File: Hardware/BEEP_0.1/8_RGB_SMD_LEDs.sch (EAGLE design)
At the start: 34 parts

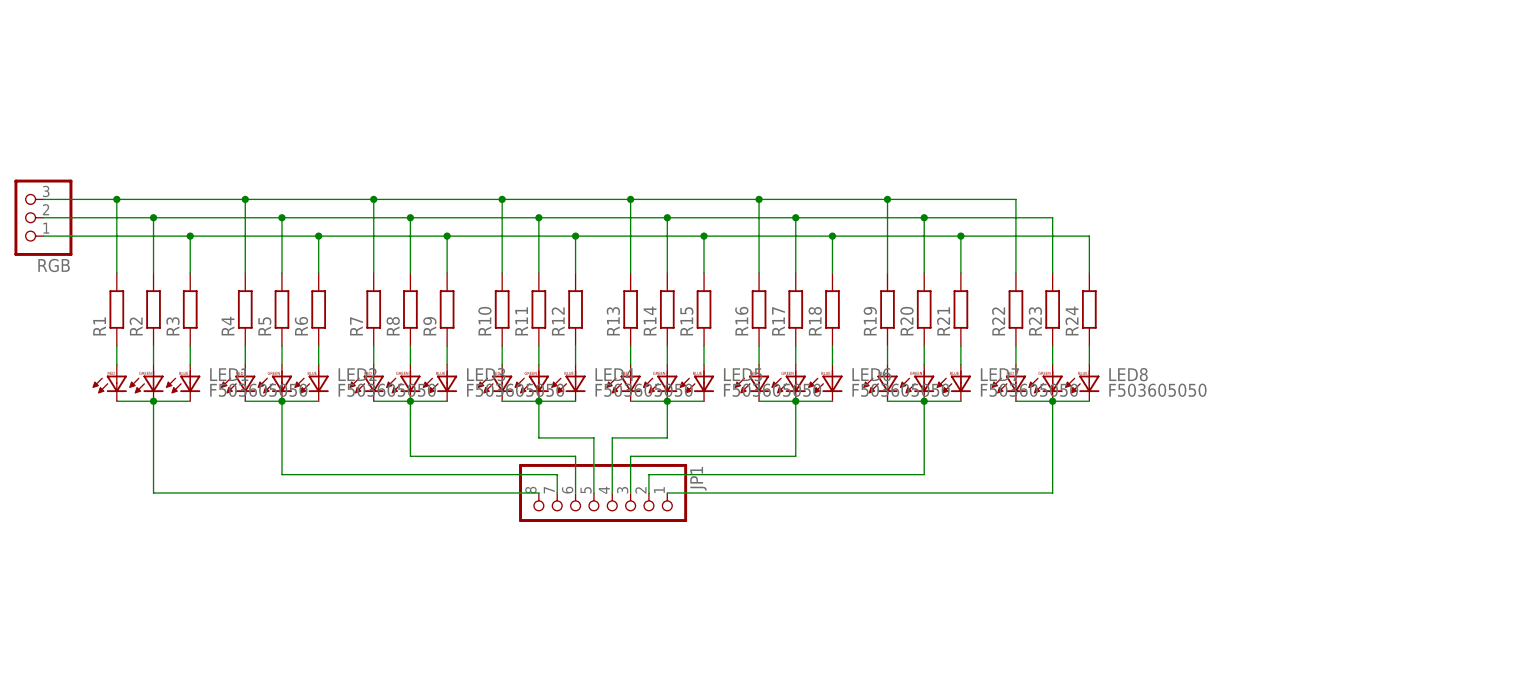
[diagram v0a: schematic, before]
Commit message: Add branding ;) enhance PCBs finish Easy RGB Board add Texas Instruments libray from Element 14 add dxf import ulp for eagle add Script for easy eagle export to pdf for etching minor cleanup
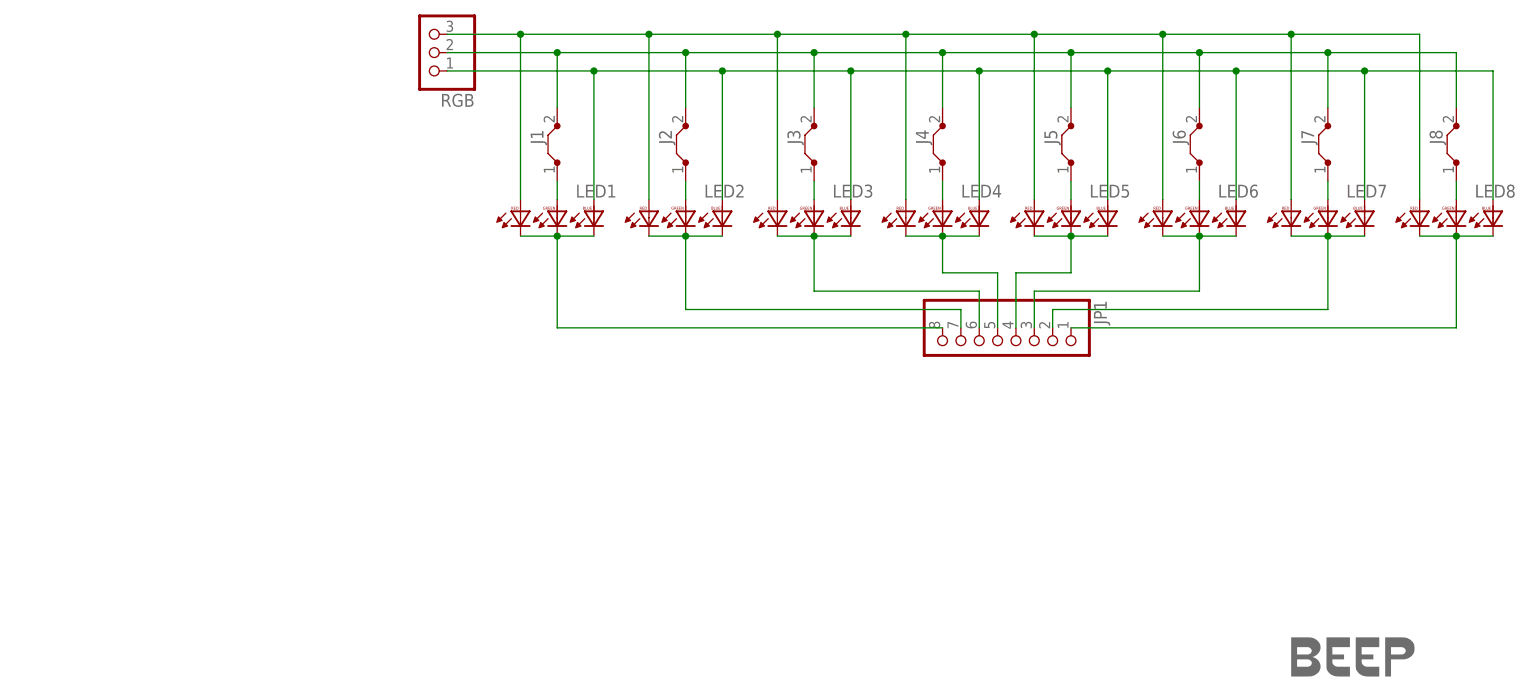
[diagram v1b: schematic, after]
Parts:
- removed R1, R10, R11, R12, R13, R14, R15, R16, R17, R18, R19, R2, R20, R21, R22, R23, R24, R3, R4, R5, R6, R7, R8, R9: (no value), rcl:R-EU_0207/7
- added J1, J2, J3, J4, J5, J6, J7, J8: J7MM, jumper:J7MM
- added U$5: LOGO-COPPER7, Branding:LOGO-COPPER7
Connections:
- removed net N$1: R1.2, R10.2, R13.2, R16.2, R19.2, R22.2, R4.2, R7.2, RGB.3
- removed net N$11: LED2.RA, R4.1
- removed net N$13: LED2.BA, R6.1
- removed net N$18: LED3.RA, R7.1
- removed net N$20: LED3.BA, R9.1
- removed net N$21: LED4.RA, R10.1
- removed net N$23: LED4.BA, R12.1
- removed net N$24: LED5.RA, R13.1
- removed net N$26: LED5.BA, R15.1
- removed net N$27: LED6.RA, R16.1
- removed net N$29: LED6.BA, R18.1
- removed net N$3: R12.2, R15.2, R18.2, R21.2, R24.2, R3.2, R6.2, R9.2, RGB.1
- removed net N$30: LED7.RA, R19.1
- removed net N$32: LED7.BA, R21.1
- removed net N$4: LED1.RA, R1.1
- removed net N$6: LED1.BA, R3.1
- net N$12: now also J2.1; no longer R5.1
- net N$19: now also J3.1; no longer R8.1
- net N$2: now also J1.2, J2.2, J3.2, J4.2, J5.2, J6.2, J7.2, J8.2; no longer R11.2, R14.2, R17.2, R2.2, R20.2, R23.2, R5.2, R8.2
- net N$22: now also J4.1; no longer R11.1
- net N$25: now also J5.1; no longer R14.1
- net N$28: now also J6.1; no longer R17.1
- net N$31: now also J7.1; no longer R20.1
- net N$33: now also LED1.RA, LED2.RA, LED3.RA, LED4.RA, LED5.RA, LED6.RA, LED7.RA, RGB.3; no longer R22.1
- net N$34: now also J8.1; no longer R23.1
- net N$35: now also LED1.BA, LED2.BA, LED3.BA, LED4.BA, LED5.BA, LED6.BA, LED7.BA, RGB.1; no longer R24.1
- net N$5: now also J1.1; no longer R2.1
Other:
- moved on the sheet: JP1, LED1, LED2, LED3, LED4, LED5, LED6, LED7, LED8, RGB
